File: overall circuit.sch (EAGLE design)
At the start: 13 parts, among them K1 RELAY-SPDT-JZC-11F, M2 MOTOR10MM, U1 ARDUINOR3-DIMENSION

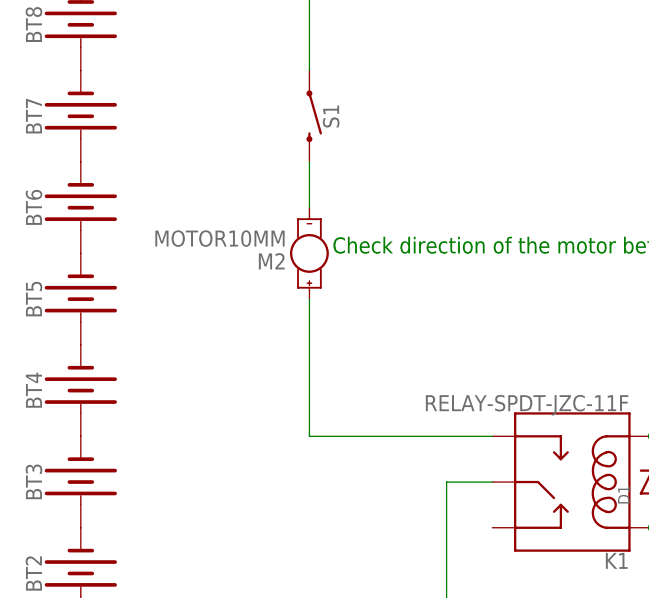
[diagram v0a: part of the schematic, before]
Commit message: Added flyback diode for the motor
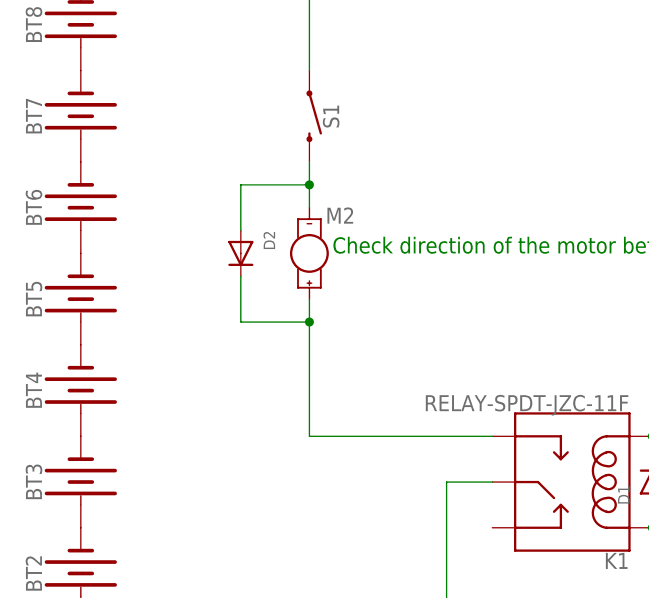
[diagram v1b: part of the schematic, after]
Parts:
- added D2: (no value), adafruit:DIODEDO-1N4148
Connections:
- net N$12: now also D2.C
- net N$13: now also D2.A
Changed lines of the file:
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@@
 <part name="M2" library="SparkFun-Electromechanical" deviceset="MOTOR" device="10MM"/>
 <part name="S1" library="SparkFun-Switches" deviceset="MOMENTARY-SWITCH-SPST" device="-SMD-5.2MM"/>
+<part name="D2" library="adafruit" deviceset="DIODE" device="DO-1N4148"/>
 </parts>
 <sheets>
@@
 <instance part="U1" gate="G$1" x="114.3" y="17.78" rot="R90"/>
 <instance part="D1" gate="G$1" x="71.12" y="10.16" rot="R90"/>
-<instance part="M2" gate="G$1" x="33.02" y="35.56" rot="R180"/>
+<instance part="M2" gate="G$1" x="33.02" y="35.56" smashed="yes" rot="R180">
+<attribute name="NAME" x="38.1" y="40.64" size="1.778" layer="95" font="vector" rot="R180"/>
+</instance>
 <instance part="S1" gate="G$1" x="33.02" y="50.8" smashed="yes" rot="R270">
 <attribute name="NAME" x="34.544" y="50.8" size="1.778" layer="95" font="vector" rot="R270" align="bottom-center"/>
 </instance>
+<instance part="D2" gate="G$1" x="25.4" y="35.56" rot="R270"/>
 </instances>
 <busses>
@@
 <wire x1="33.02" y1="15.24" x2="53.34" y2="15.24" width="0.1524" layer="91"/>
 <pinref part="M2" gate="G$1" pin="+"/>
-<wire x1="33.02" y1="30.48" x2="33.02" y2="15.24" width="0.1524" layer="91"/>
+<wire x1="33.02" y1="30.48" x2="33.02" y2="27.94" width="0.1524" layer="91"/>
+<pinref part="D2" gate="G$1" pin="C"/>
+<wire x1="33.02" y1="27.94" x2="33.02" y2="15.24" width="0.1524" layer="91"/>
+<wire x1="25.4" y1="33.02" x2="25.4" y2="27.94" width="0.1524" layer="91"/>
+<wire x1="25.4" y1="27.94" x2="33.02" y2="27.94" width="0.1524" layer="91"/>
+<junction x="33.02" y="27.94"/>
 </segment>
 </net>
@@
 <pinref part="S1" gate="G$1" pin="2"/>
 <pinref part="M2" gate="G$1" pin="-"/>
-<wire x1="33.02" y1="45.72" x2="33.02" y2="40.64" width="0.1524" layer="91"/>
+<wire x1="33.02" y1="45.72" x2="33.02" y2="43.18" width="0.1524" layer="91"/>
+<pinref part="D2" gate="G$1" pin="A"/>
+<wire x1="33.02" y1="43.18" x2="33.02" y2="40.64" width="0.1524" layer="91"/>
+<wire x1="33.02" y1="43.18" x2="25.4" y2="43.18" width="0.1524" layer="91"/>
+<wire x1="25.4" y1="43.18" x2="25.4" y2="38.1" width="0.1524" layer="91"/>
+<junction x="33.02" y="43.18"/>
 </segment>
 </net>

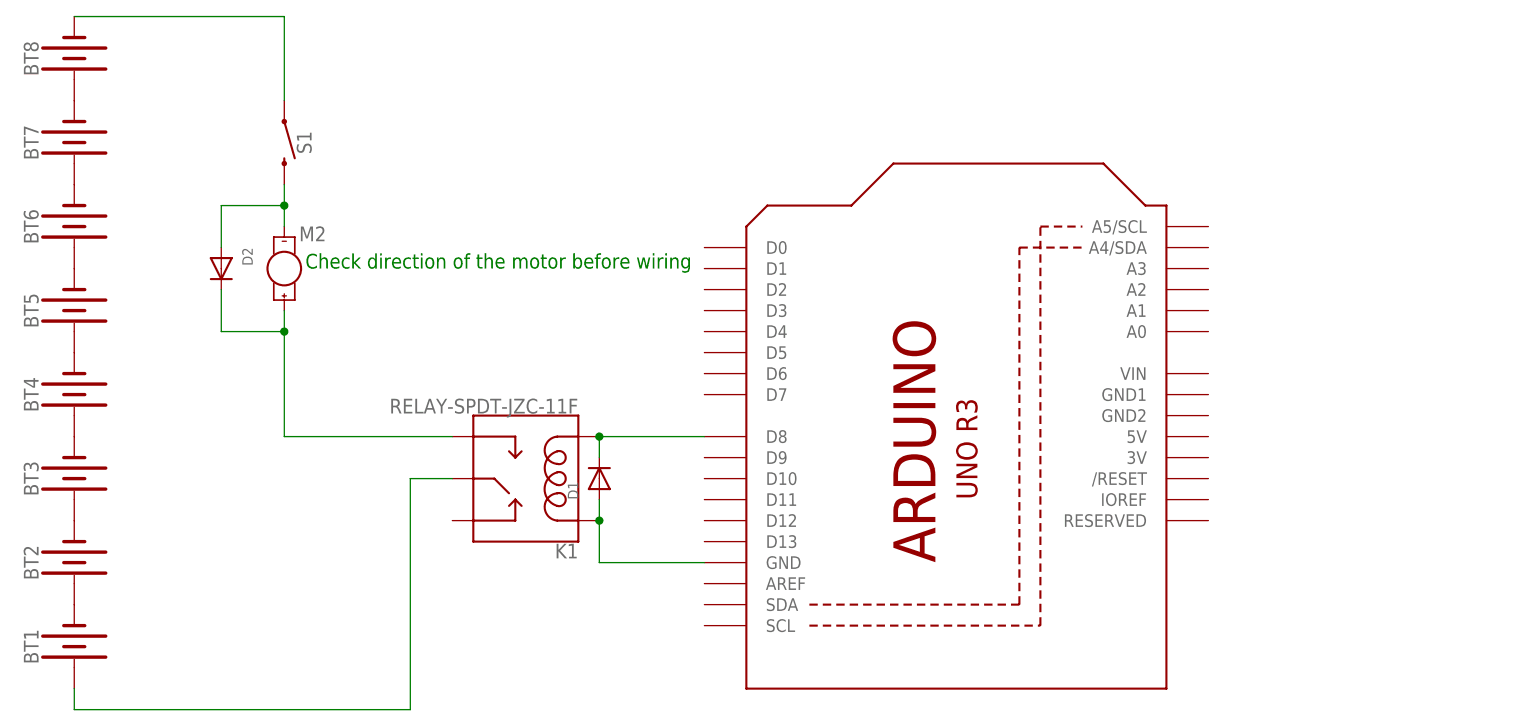
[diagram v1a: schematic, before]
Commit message: New circuit with terminal and diode
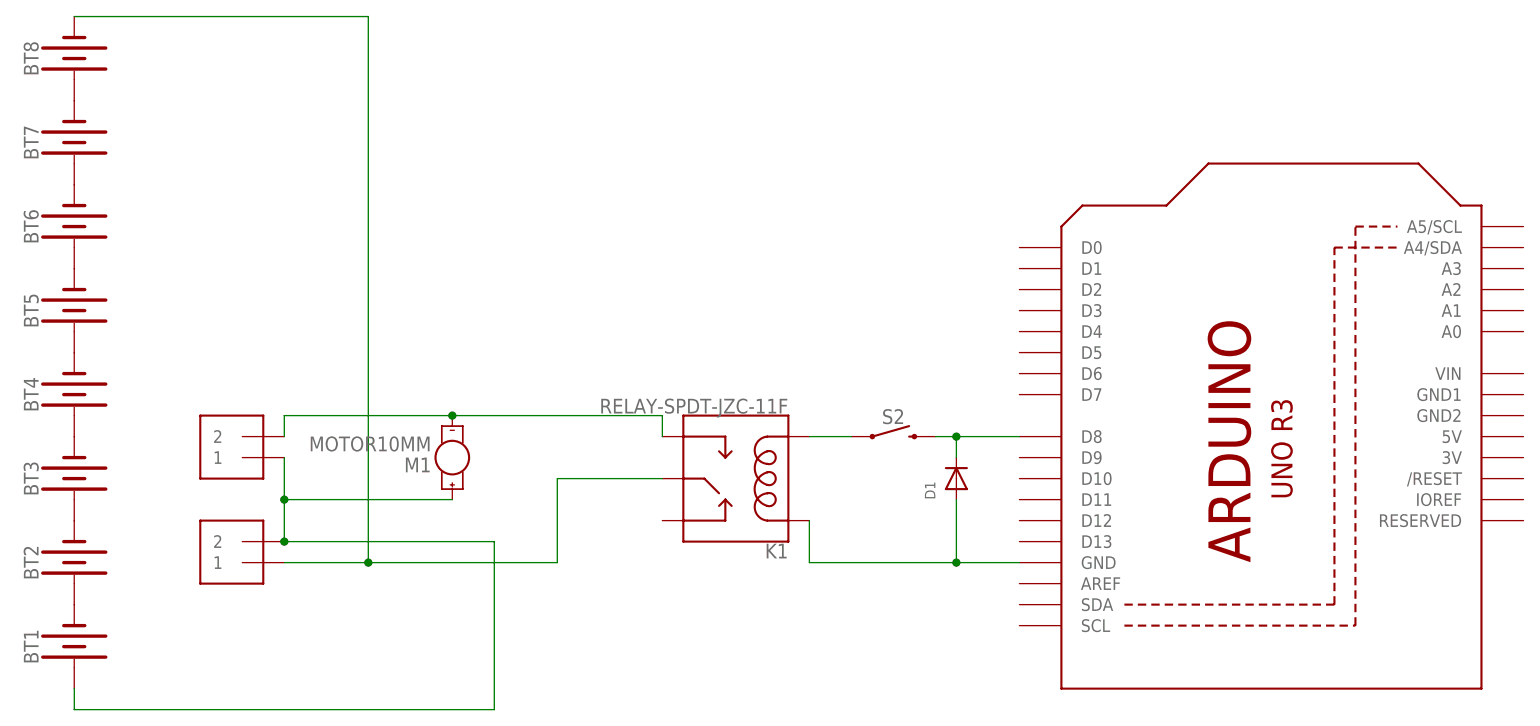
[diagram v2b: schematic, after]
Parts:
- removed D2: (no value), adafruit:DIODEDO-1N4148
- removed M2: MOTOR10MM, SparkFun-Electromechanical:MOTOR10MM
- removed S1: MOMENTARY-SWITCH-SPST-SMD-5.2MM, SparkFun-Switches:MOMENTARY-SWITCH-SPST-SMD-5.2MM
- added J1, J2: 1X2-3.5MM, adafruit:1X2-3.5MM
- added M1: MOTOR10MM, SparkFun-Electromechanical:MOTOR10MM
- added S2: MOMENTARY-SWITCH-SPST-SMD-5.2MM, SparkFun-Switches:MOMENTARY-SWITCH-SPST-SMD-5.2MM
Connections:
- removed net N$11 (its old number): BT1.+, K1.MAIN
- removed net N$13: D2.A, M2.-, S1.2
- new net N$15: D1.C, S2.2, U1.D8
- new net N$9: J1.2, K1.NO, M1.-
- net N$10: now also J2.1, K1.MAIN; no longer S1.1
- net N$12: now also BT1.+, J1.1, J2.2, M1.+; no longer D2.C, K1.NO, M2.+
- net N$8: now also S2.1; no longer D1.C, U1.D8
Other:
- note removed: "Check direction of the motor before wiring"
- moved on the sheet: D1, K1
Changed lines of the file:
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@@
 <part name="BT8" library="SparkFun-Batteries" deviceset="BATTERY" device="-9V"/>
 <part name="K1" library="SparkFun-Electromechanical" deviceset="RELAY-SPDT" device="-JZC-11F"/>
+<part name="M1" library="SparkFun-Electromechanical" deviceset="MOTOR" device="10MM"/>
 <part name="U1" library="adafruit" deviceset="ARDUINOR3" device="-DIMENSION"/>
+<part name="S2" library="SparkFun-Switches" deviceset="MOMENTARY-SWITCH-SPST" device="-SMD-5.2MM"/>
+<part name="J1" library="adafruit" deviceset="1X2" device="-3.5MM"/>
+<part name="J2" library="adafruit" deviceset="1X2" device="-3.5MM"/>
 <part name="D1" library="adafruit" deviceset="DIODE" device="DO-1N4148"/>
-<part name="M2" library="SparkFun-Electromechanical" deviceset="MOTOR" device="10MM"/>
-<part name="S1" library="SparkFun-Switches" deviceset="MOMENTARY-SWITCH-SPST" device="-SMD-5.2MM"/>
-<part name="D2" library="adafruit" deviceset="DIODE" device="DO-1N4148"/>
 </parts>
 <sheets>
 <sheet>
 <plain>
-<text x="35.56" y="35.56" size="1.778" layer="91">Check direction of the motor before wiring</text>
 </plain>
 <instances>
@@
 <instance part="BT7" gate="G$1" x="7.62" y="50.8" rot="R90"/>
 <instance part="BT8" gate="G$1" x="7.62" y="60.96" rot="R90"/>
-<instance part="K1" gate="K$1" x="60.96" y="10.16" rot="R180"/>
-<instance part="U1" gate="G$1" x="114.3" y="17.78" rot="R90"/>
-<instance part="D1" gate="G$1" x="71.12" y="10.16" rot="R90"/>
-<instance part="M2" gate="G$1" x="33.02" y="35.56" smashed="yes" rot="R180">
-<attribute name="NAME" x="38.1" y="40.64" size="1.778" layer="95" font="vector" rot="R180"/>
+<instance part="K1" gate="K$1" x="86.36" y="10.16" rot="R180"/>
+<instance part="M1" gate="G$1" x="53.34" y="12.7" rot="R180"/>
+<instance part="U1" gate="G$1" x="152.4" y="17.78" rot="R90"/>
+<instance part="S2" gate="G$1" x="106.68" y="15.24" smashed="yes">
+<attribute name="NAME" x="106.68" y="16.764" size="1.778" layer="95" font="vector" align="bottom-center"/>
 </instance>
-<instance part="S1" gate="G$1" x="33.02" y="50.8" smashed="yes" rot="R270">
-<attribute name="NAME" x="34.544" y="50.8" size="1.778" layer="95" font="vector" rot="R270" align="bottom-center"/>
-</instance>
-<instance part="D2" gate="G$1" x="25.4" y="35.56" rot="R270"/>
+<instance part="J1" gate="G$1" x="27.94" y="15.24" rot="R180"/>
+<instance part="J2" gate="G$1" x="27.94" y="2.54" rot="R180"/>
+<instance part="D1" gate="G$1" x="114.3" y="10.16" rot="R90"/>
 </instances>
 <busses>
@@
 </segment>
 </net>
+<net name="N$12" class="0">
+<segment>
+<pinref part="BT1" gate="G$1" pin="+"/>
+<wire x1="7.62" y1="-17.78" x2="7.62" y2="-15.24" width="0.1524" layer="91"/>
+<wire x1="7.62" y1="-17.78" x2="58.42" y2="-17.78" width="0.1524" layer="91"/>
+<wire x1="58.42" y1="-17.78" x2="58.42" y2="2.54" width="0.1524" layer="91"/>
+<pinref part="J2" gate="G$1" pin="2"/>
+<wire x1="58.42" y1="2.54" x2="33.02" y2="2.54" width="0.1524" layer="91"/>
+<pinref part="M1" gate="G$1" pin="+"/>
+<pinref part="J1" gate="G$1" pin="1"/>
+<wire x1="53.34" y1="7.62" x2="33.02" y2="7.62" width="0.1524" layer="91"/>
+<wire x1="33.02" y1="7.62" x2="33.02" y2="12.7" width="0.1524" layer="91"/>
+<wire x1="33.02" y1="2.54" x2="33.02" y2="7.62" width="0.1524" layer="91"/>
+<junction x="33.02" y="2.54"/>
+<junction x="33.02" y="7.62"/>
+</segment>
+</net>
+<net name="N$8" class="0">
+<segment>
+<pinref part="K1" gate="K$1" pin="COIL2"/>
+<pinref part="S2" gate="G$1" pin="1"/>
+<wire x1="101.6" y1="15.24" x2="96.52" y2="15.24" width="0.1524" layer="91"/>
+</segment>
+</net>
+<net name="N$15" class="0">
+<segment>
+<pinref part="S2" gate="G$1" pin="2"/>
+<pinref part="U1" gate="G$1" pin="D8"/>
+<wire x1="111.76" y1="15.24" x2="114.3" y2="15.24" width="0.1524" layer="91"/>
+<pinref part="D1" gate="G$1" pin="C"/>
+<wire x1="114.3" y1="15.24" x2="121.92" y2="15.24" width="0.1524" layer="91"/>
+<wire x1="114.3" y1="12.7" x2="114.3" y2="15.24" width="0.1524" layer="91"/>
+<junction x="114.3" y="15.24"/>
+</segment>
+</net>
 <net name="N$9" class="0">
 <segment>
-<pinref part="K1" gate="K$1" pin="COIL1"/>
-<wire x1="71.12" y1="5.08" x2="71.12" y2="0" width="0.1524" layer="91"/>
-<pinref part="U1" gate="G$1" pin="GND"/>
-<wire x1="71.12" y1="0" x2="83.82" y2="0" width="0.1524" layer="91"/>
-<pinref part="D1" gate="G$1" pin="A"/>
-<wire x1="71.12" y1="7.62" x2="71.12" y2="5.08" width="0.1524" layer="91"/>
-<junction x="71.12" y="5.08"/>
+<pinref part="M1" gate="G$1" pin="-"/>
+<pinref part="J1" gate="G$1" pin="2"/>
+<wire x1="53.34" y1="17.78" x2="33.02" y2="17.78" width="0.1524" layer="91"/>
+<wire x1="33.02" y1="17.78" x2="33.02" y2="15.24" width="0.1524" layer="91"/>
+<pinref part="K1" gate="K$1" pin="NO"/>
+<wire x1="53.34" y1="17.78" x2="78.74" y2="17.78" width="0.1524" layer="91"/>
+<wire x1="78.74" y1="17.78" x2="78.74" y2="15.24" width="0.1524" layer="91"/>
+<junction x="53.34" y="17.78"/>
 </segment>
 </net>
@@
 <segment>
 <pinref part="BT8" gate="G$1" pin="-"/>
-<wire x1="7.62" y1="66.04" x2="33.02" y2="66.04" width="0.1524" layer="91"/>
-<pinref part="S1" gate="G$1" pin="1"/>
-<wire x1="33.02" y1="66.04" x2="33.02" y2="55.88" width="0.1524" layer="91"/>
+<wire x1="7.62" y1="66.04" x2="43.18" y2="66.04" width="0.1524" layer="91"/>
+<pinref part="K1" gate="K$1" pin="MAIN"/>
+<wire x1="78.74" y1="10.16" x2="66.04" y2="10.16" width="0.1524" layer="91"/>
+<pinref part="J2" gate="G$1" pin="1"/>
+<wire x1="33.02" y1="0" x2="43.18" y2="0" width="0.1524" layer="91"/>
+<wire x1="43.18" y1="0" x2="66.04" y2="0" width="0.1524" layer="91"/>
+<wire x1="66.04" y1="0" x2="66.04" y2="10.16" width="0.1524" layer="91"/>
+<wire x1="43.18" y1="66.04" x2="43.18" y2="0" width="0.1524" layer="91"/>
+<junction x="43.18" y="0"/>
 </segment>
 </net>
 <net name="N$11" class="0">
 <segment>
-<pinref part="K1" gate="K$1" pin="MAIN"/>
-<wire x1="53.34" y1="10.16" x2="48.26" y2="10.16" width="0.1524" layer="91"/>
-<wire x1="48.26" y1="-17.78" x2="48.26" y2="10.16" width="0.1524" layer="91"/>
-<pinref part="BT1" gate="G$1" pin="+"/>
-<wire x1="7.62" y1="-17.78" x2="7.62" y2="-15.24" width="0.1524" layer="91"/>
-<wire x1="7.62" y1="-17.78" x2="48.26" y2="-17.78" width="0.1524" layer="91"/>
+<pinref part="K1" gate="K$1" pin="COIL1"/>
+<wire x1="96.52" y1="5.08" x2="96.52" y2="0" width="0.1524" layer="91"/>
+<pinref part="U1" gate="G$1" pin="GND"/>
+<wire x1="96.52" y1="0" x2="114.3" y2="0" width="0.1524" layer="91"/>
+<pinref part="D1" gate="G$1" pin="A"/>
+<wire x1="114.3" y1="0" x2="121.92" y2="0" width="0.1524" layer="91"/>
+<wire x1="114.3" y1="7.62" x2="114.3" y2="0" width="0.1524" layer="91"/>
+<junction x="114.3" y="0"/>
 </segment>
 </net>
-<net name="N$8" class="0">
-<segment>
-<pinref part="K1" gate="K$1" pin="COIL2"/>
-<pinref part="D1" gate="G$1" pin="C"/>
-<wire x1="71.12" y1="12.7" x2="71.12" y2="15.24" width="0.1524" layer="91"/>
-<pinref part="U1" gate="G$1" pin="D8"/>
-<wire x1="71.12" y1="15.24" x2="83.82" y2="15.24" width="0.1524" layer="91"/>
-<junction x="71.12" y="15.24"/>
-</segment>
-</net>
-<net name="N$12" class="0">
-<segment>
-<pinref part="K1" gate="K$1" pin="NO"/>
-<wire x1="33.02" y1="15.24" x2="53.34" y2="15.24" width="0.1524" layer="91"/>
-<pinref part="M2" gate="G$1" pin="+"/>
-<wire x1="33.02" y1="30.48" x2="33.02" y2="27.94" width="0.1524" layer="91"/>
-<pinref part="D2" gate="G$1" pin="C"/>
-<wire x1="33.02" y1="27.94" x2="33.02" y2="15.24" width="0.1524" layer="91"/>
-<wire x1="25.4" y1="33.02" x2="25.4" y2="27.94" width="0.1524" layer="91"/>
-<wire x1="25.4" y1="27.94" x2="33.02" y2="27.94" width="0.1524" layer="91"/>
-<junction x="33.02" y="27.94"/>
-</segment>
-</net>
-<net name="N$13" class="0">
-<segment>
-<pinref part="S1" gate="G$1" pin="2"/>
-<pinref part="M2" gate="G$1" pin="-"/>
-<wire x1="33.02" y1="45.72" x2="33.02" y2="43.18" width="0.1524" layer="91"/>
-<pinref part="D2" gate="G$1" pin="A"/>
-<wire x1="33.02" y1="43.18" x2="33.02" y2="40.64" width="0.1524" layer="91"/>
-<wire x1="33.02" y1="43.18" x2="25.4" y2="43.18" width="0.1524" layer="91"/>
-<wire x1="25.4" y1="43.18" x2="25.4" y2="38.1" width="0.1524" layer="91"/>
-<junction x="33.02" y="43.18"/>
-</segment>
-</net>
